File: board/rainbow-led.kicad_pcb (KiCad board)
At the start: 2 copper layers, 25.5 x 11.5 mm, 9 parts, among them J1 Conn_01x04, J2 Conn_01x06, J3 Conn_01x02, SW1 SW_Push, U1 TPS61222DCKR, U3 ATtiny85-20S

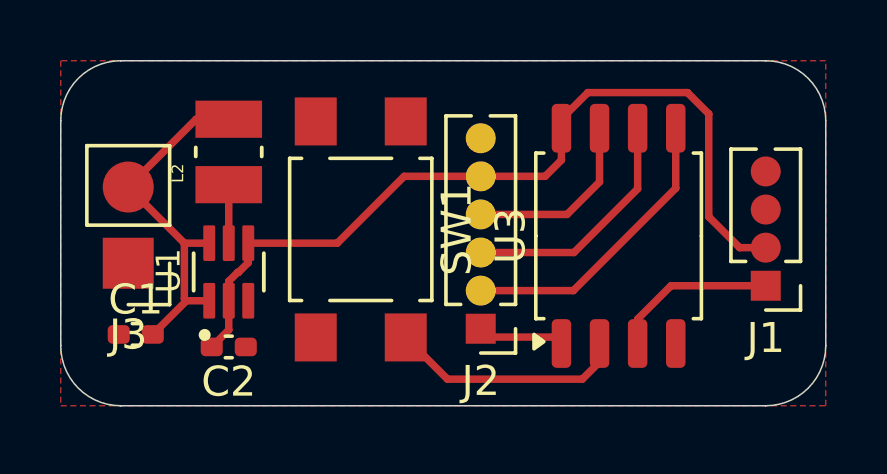
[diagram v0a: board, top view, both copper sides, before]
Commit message: Switch inductor to recommended one.
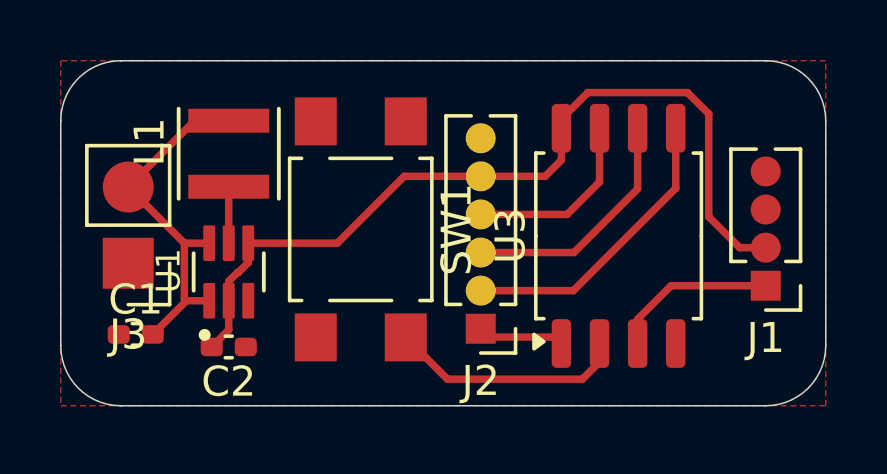
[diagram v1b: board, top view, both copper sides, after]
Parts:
- removed L2: 4.7u, LQM2HPN4R7MG0L:INDC2520X100N
- added L1: LQH3NPN4R7MMEL, LQH3NPN4R7MMELCT:IND_LQH3NPN4R7MMEL, F.Cu at (103.6, 66.1)
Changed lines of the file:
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@@
 		)
+	)
+	(footprint "LQH3NPN4R7MMELCT:IND_LQH3NPN4R7MMEL"
+		(layer "F.Cu")
+		(at 103.6 66.1 90)
+		(property "Reference" "L1"
+			(at 0.395 -2.635 90)
+			(layer "F.SilkS")
+			(effects
+				(font
+					(size 1 1)
+					(thickness 0.15)
+				)
+			)
+		)
+		(property "Value" "LQH3NPN4R7MMEL"
+			(at 8.65 2.635 90)
+			(layer "F.Fab")
+			(effects
+				(font
+					(size 1 1)
+					(thickness 0.15)
+				)
+			)
+		)
+		(property "Datasheet" ""
+			(at 0 0 90)
+			(layer "F.Fab")
+			(hide yes)
+			(effects
+				(font
+					(size 1.27 1.27)
+					(thickness 0.15)
+				)
+			)
+		)
+		(property "Description" ""
+			(at 0 0 90)
+			(layer "F.Fab")
+			(hide yes)
+			(effects
+				(font
+					(size 1.27 1.27)
+					(thickness 0.15)
+				)
+			)
+		)
+		(property "PARTREV" "N/A"
+			(at 0 0 90)
+			(unlocked yes)
+			(layer "F.Fab")
+			(hide yes)
+			(effects
+				(font
+					(size 1 1)
+					(thickness 0.15)
+				)
+			)
+		)
+		(property "MANUFACTURER" "Murata"
+			(at 0 0 90)
+			(unlocked yes)
+			(layer "F.Fab")
+			(hide yes)
+			(effects
+				(font
+					(size 1 1)
+					(thickness 0.15)
+				)
+			)
+		)
+		(property "MAXIMUM_PACKAGE_HEIGHT" "1.5mm"
+			(at 0 0 90)
+			(unlocked yes)
+			(layer "F.Fab")
+			(hide yes)
+			(effects
+				(font
+					(size 1 1)
+					(thickness 0.15)
+				)
+			)
+		)
+		(property "STANDARD" "Manufacturer Recommendations"
+			(at 0 0 90)
+			(unlocked yes)
+			(layer "F.Fab")
+			(hide yes)
+			(effects
+				(font
+					(size 1 1)
+					(thickness 0.15)
+				)
+			)
+		)
+		(sheetname "/")
+		(sheetfile "rainbow-led.kicad_sch")
+		(attr smd)
+		(fp_line
+			(start -1.5 -1.67)
+			(end 1.5 -1.67)
+			(stroke
+				(width 0.127)
+				(type solid)
+			)
+			(layer "F.SilkS")
+		)
+		(fp_line
+			(start -1.5 1.67)
+			(end 1.5 1.67)
+			(stroke
+				(width 0.127)
+				(type solid)
+			)
+			(layer "F.SilkS")
+		)
+		(fp_line
+			(start 1.75 -1.75)
+			(end 1.75 1.75)
+			(stroke
+				(width 0.05)
+				(type solid)
+			)
+			(layer "F.CrtYd")
+		)
+		(fp_line
+			(start -1.75 -1.75)
+			(end 1.75 -1.75)
+			(stroke
+				(width 0.05)
+				(type solid)
+			)
+			(layer "F.CrtYd")
+		)
+		(fp_line
+			(start 1.75 1.75)
+			(end -1.75 1.75)
+			(stroke
+				(width 0.05)
+				(type solid)
+			)
+			(layer "F.CrtYd")
+		)
+		(fp_line
+			(start -1.75 1.75)
+			(end -1.75 -1.75)
+			(stroke
+				(width 0.05)
+				(type solid)
+			)
+			(layer "F.CrtYd")
+		)
+		(fp_line
+			(start 1.5 -1.5)
+			(end 1.5 1.5)
+			(stroke
+				(width 0.127)
+				(type solid)
+			)
+			(layer "F.Fab")
+		)
+		(fp_line
+			(start -1.5 -1.5)
+			(end 1.5 -1.5)
+			(stroke
+				(width 0.127)
+				(type solid)
+			)
+			(layer "F.Fab")
+		)
+		(fp_line
+			(start 1.5 1.5)
+			(end -1.5 1.5)
+			(stroke
+				(width 0.127)
+				(type solid)
+			)
+			(layer "F.Fab")
+		)
+		(fp_line
+			(start -1.5 1.5)
+			(end -1.5 -1.5)
+			(stroke
+				(width 0.127)
+				(type solid)
+			)
+			(layer "F.Fab")
+		)
+		(pad "1" smd rect
+			(at -1.1 0 90)
+			(size 0.8 2.7)
+			(layers "F.Cu" "F.Mask" "F.Paste")
+			(net 10 "Net-(U1-L)")
+			(pintype "passive")
+			(solder_mask_margin 0.102)
+		)
+		(pad "2" smd rect
+			(at 1.1 0 90)
+			(size 0.8 2.7)
+			(layers "F.Cu" "F.Mask" "F.Paste")
+			(net 1 "+BATT")
+			(pintype "passive")
+			(solder_mask_margin 0.102)
+		)
+		(embedded_fonts no)
 	)
 	(footprint "Capacitor_SMD:C_0402_1005Metric_Pad0.74x0.62mm_HandSolder"
@@
 		)
 	)
-	(footprint "LQM2HPN4R7MG0L:INDC2520X100N"
-		(layer "F.Cu")
-		(at 103.6 66.04 90)
-		(property "Reference" "L2"
-			(at -0.71 -1.7 90)
-			(layer "F.SilkS")
-			(effects
-				(font
-					(size 0.393701 0.393701)
-					(thickness 0.15)
-				)
-			)
-		)
-		(property "Value" "4.7u"
-			(at 1.29 1.7 90)
-			(layer "F.Fab")
-			(effects
-				(font
-					(size 0.393701 0.393701)
-					(thickness 0.15)
-				)
-			)
-		)
-		(property "Datasheet" ""
-			(at 0 0 90)
-			(layer "F.Fab")
-			(hide yes)
-			(effects
-				(font
-					(size 1.27 1.27)
-					(thickness 0.15)
-				)
-			)
-		)
-		(property "Description" ""
-			(at 0 0 90)
-			(layer "F.Fab")
-			(hide yes)
-			(effects
-				(font
-					(size 1.27 1.27)
-					(thickness 0.15)
-				)
-			)
-		)
-		(sheetname "/")
-		(sheetfile "rainbow-led.kicad_sch")
-		(attr smd)
-		(fp_line
-			(start -0.15 -1.1)
-			(end 0.15 -1.1)
-			(stroke
-				(width 0.127)
-				(type solid)
-			)
-			(layer "F.SilkS")
-		)
-		(fp_line
-			(start -0.15 1.1)
-			(end 0.15 1.1)
-			(stroke
-				(width 0.127)
-				(type solid)
-			)
-			(layer "F.SilkS")
-		)
-		(fp_line
-			(start -1.958 -1.358)
-			(end 1.958 -1.358)
-			(stroke
-				(width 0.05)
-				(type solid)
-			)
-			(layer "F.CrtYd")
-		)
-		(fp_line
-			(start 1.958 1.358)
-			(end 1.958 -1.358)
-			(stroke
-				(width 0.05)
-				(type solid)
-			)
-			(layer "F.CrtYd")
-		)
-		(fp_line
-			(start -1.958 1.358)
-			(end -1.958 -1.358)
-			(stroke
-				(width 0.05)
-				(type solid)
-			)
-			(layer "F.CrtYd")
-		)
-		(fp_line
-			(start -1.958 1.358)
-			(end 1.958 1.358)
-			(stroke
-				(width 0.05)
-				(type solid)
-			)
-			(layer "F.CrtYd")
-		)
-		(fp_line
-			(start 1.35 -1.1)
-			(end -1.35 -1.1)
-			(stroke
-				(width 0.127)
-				(type solid)
-			)
-			(layer "F.Fab")
-		)
-		(fp_line
-			(start 1.35 1.1)
-			(end 1.35 -1.1)
-			(stroke
-				(width 0.127)
-				(type solid)
-			)
-			(layer "F.Fab")
-		)
-		(fp_line
-			(start 1.35 1.1)
-			(end -1.35 1.1)
-			(stroke
-				(width 0.127)
-				(type solid)
-			)
-			(layer "F.Fab")
-		)
-		(fp_line
-			(start -1.35 1.1)
-			(end -1.35 -1.1)
-			(stroke
-				(width 0.127)
-				(type solid)
-			)
-			(layer "F.Fab")
-		)
-		(pad "1" smd rect
-			(at -1.09 0 90)
-			(size 1.24 2.22)
-			(layers "F.Cu" "F.Mask" "F.Paste")
-			(net 10 "Net-(U1-L)")
-			(pintype "passive")
-			(solder_mask_margin 0.102)
-		)
-		(pad "2" smd rect
-			(at 1.09 0 90)
-			(size 1.24 2.22)
-			(layers "F.Cu" "F.Mask" "F.Paste")
-			(net 1 "+BATT")
-			(pintype "passive")
-			(solder_mask_margin 0.102)
-		)
-		(embedded_fonts no)
-	)
 	(footprint "Connectors:Pads_1x06_P1.27mm"
